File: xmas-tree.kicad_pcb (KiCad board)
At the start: 2 copper layers, 130.1 x 110 mm, 28 parts, among them U1 SN74HCS594, U2 LM555xM, U3 74AHC1G32

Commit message: Initial Commit
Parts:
- removed REF**: MountingHole_3.2mm_M3_DIN965_Pad, MountingHole:MountingHole_3.2mm_M3_DIN965_Pad
- C1: renamed from C2; value 0.1uf -> 0.01uf; footprint Capacitor_SMD:C_1210_3225Metric_Pad1.33x2.70mm_HandSolder -> Capacitor_SMD:C_0805_2012Metric_Pad1.18x1.45mm_HandSolder
- C2: renamed from C1; footprint Capacitor_SMD:C_1210_3225Metric_Pad1.33x2.70mm_HandSolder -> Capacitor_SMD:C_0805_2012Metric_Pad1.18x1.45mm_HandSolder
- C3: value C_Small -> 22uf; footprint Capacitor_SMD:C_1210_3225Metric_Pad1.33x2.70mm_HandSolder -> Capacitor_SMD:C_0805_2012Metric_Pad1.18x1.45mm_HandSolder
- D8: renamed from D4; moved to B.Cu
- R1: renamed from R7; footprint Resistor_SMD:R_2010_5025Metric -> Resistor_SMD:R_0805_2012Metric_Pad1.20x1.40mm_HandSolder
- R10: renamed from R6; value R_US -> 13K; footprint Resistor_SMD:R_2010_5025Metric_Pad1.40x2.65mm_HandSolder -> Resistor_SMD:R_0805_2012Metric_Pad1.20x1.40mm_HandSolder
- R2, R5: footprint Resistor_SMD:R_2010_5025Metric -> Resistor_SMD:R_0805_2012Metric_Pad1.20x1.40mm_HandSolder
- R3: renamed from R1; footprint Resistor_SMD:R_2010_5025Metric -> Resistor_SMD:R_0805_2012Metric_Pad1.20x1.40mm_HandSolder
- R4: renamed from R3; footprint Resistor_SMD:R_2010_5025Metric -> Resistor_SMD:R_0805_2012Metric_Pad1.20x1.40mm_HandSolder
- R6: renamed from R8; footprint Resistor_SMD:R_2010_5025Metric -> Resistor_SMD:R_0805_2012Metric_Pad1.20x1.40mm_HandSolder
- R7: renamed from R10; footprint Resistor_SMD:R_2010_5025Metric -> Resistor_SMD:R_0805_2012Metric_Pad1.20x1.40mm_HandSolder
- R8: renamed from R4; footprint Resistor_SMD:R_2010_5025Metric -> Resistor_SMD:R_0805_2012Metric_Pad1.20x1.40mm_HandSolder
- R9: value R_US -> 0; footprint Resistor_SMD:R_2010_5025Metric_Pad1.40x2.65mm_HandSolder -> Resistor_SMD:R_0805_2012Metric_Pad1.20x1.40mm_HandSolder
- turned D8 to 0 degrees
- renumbered D6 to D1, D1 to D2, D2 to D4, D7 to D6, D8 to D7
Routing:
- net LED_G: track 63.8 -> 71.4 mm
- net LED_F: track 59.3 -> 56.9 mm
- net Net-(C3-Pad1): track 27.1 -> 29.4 mm
- net LED_A: track 37.7 -> 35.9 mm
- net LED_H: track 18.4 -> 19.5 mm
- net VCC: track 152.0 -> 152.9 mm
- net Net-(R10-Pad1): track 19.4 -> 18.5 mm
- net Net-(D5-Pad2): track 5.98 -> 5.44 mm
- net Net-(D4-Pad2): track 5.07 -> 4.53 mm
- net Net-(D3-Pad2): track 5.71 -> 5.17 mm
- net LED_D: track 16.8 -> 16.3 mm
- net Net-(D8-Pad2): track 5.53 -> 4.99 mm
- net Net-(D7-Pad2): track 5.53 -> 4.99 mm
- net Net-(D6-Pad2): track 5.92 -> 5.37 mm
- net Net-(D2-Pad2): track 5.53 -> 4.99 mm
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
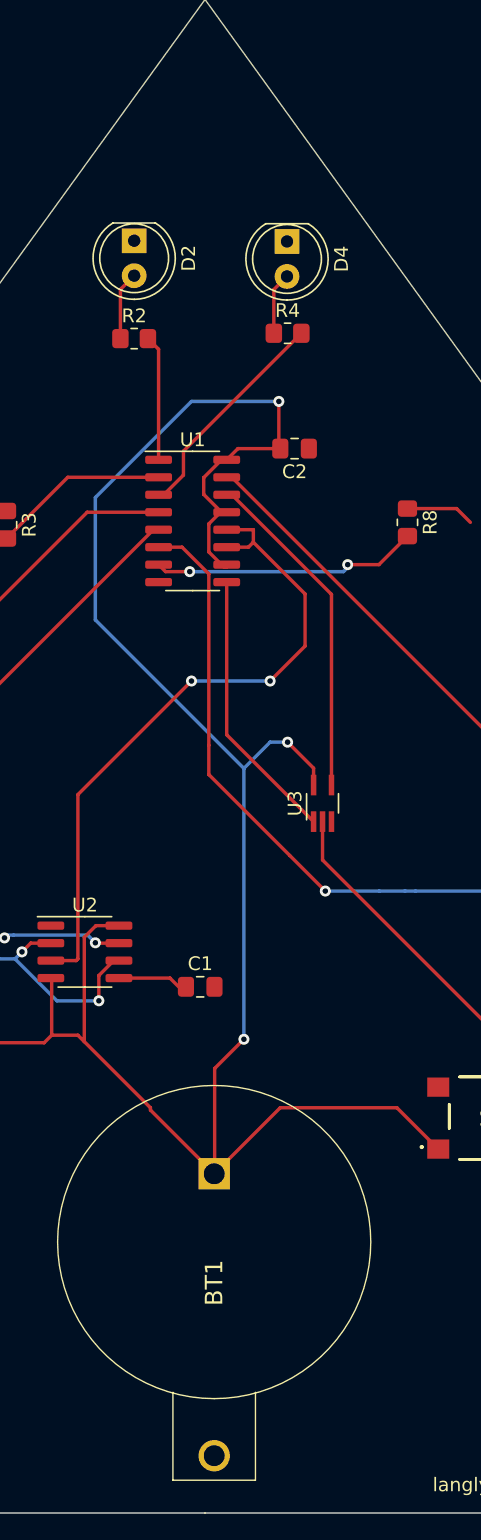
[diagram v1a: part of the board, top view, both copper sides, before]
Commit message: Fixed the problem of the battery holder being the wrong way
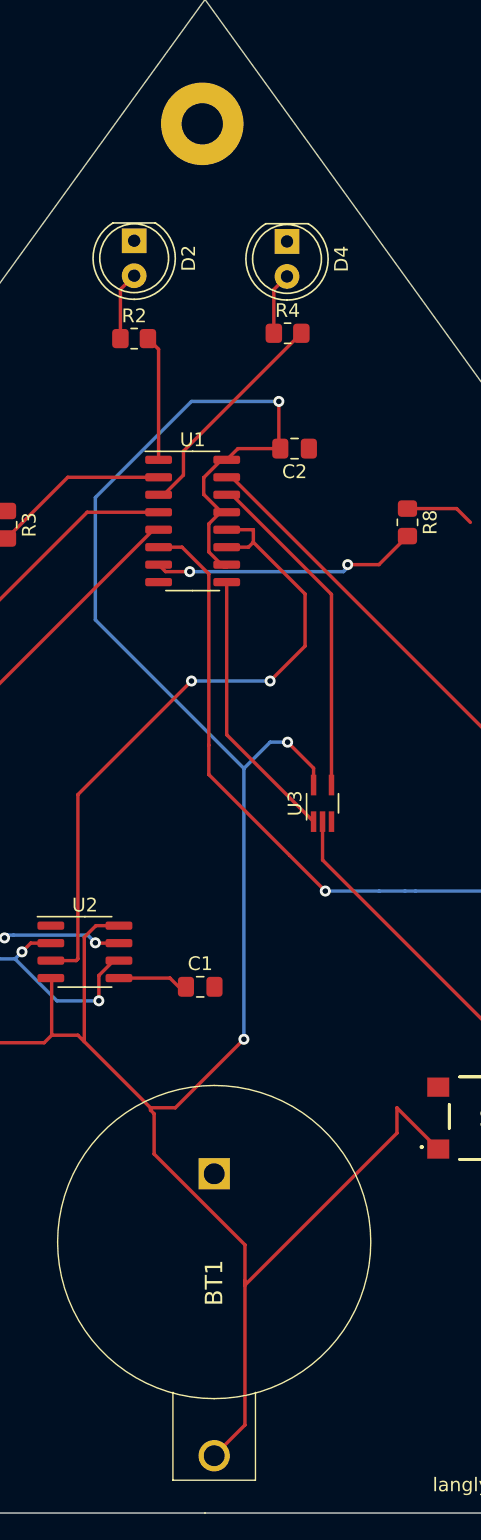
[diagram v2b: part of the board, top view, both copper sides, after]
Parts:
- added REF**: MountingHole_3mm_Pad, MountingHole:MountingHole_3mm_Pad, F.Cu at (158.5, 49.2)
- R9: value 0 -> 2k
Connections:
- BT1 pad 1: VCC -> GND
- BT1 pad 2: GND -> VCC
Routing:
- net VCC: track 152.9 -> 176.0 mm
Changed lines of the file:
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@@
     (fp_arc (start 16.34 0) (mid 4.96 11.38) (end -6.42 0) (layer "F.Fab") (width 0.2))
     (pad "1" thru_hole rect locked (at 0 0 270) (size 2.28 2.28) (drill 1.52) (layers *.Cu *.Mask)
-      (net 1 "VCC") (pinfunction "+") (pintype "passive"))
+      (net 2 "GND") (pinfunction "+") (pintype "passive"))
     (pad "2" thru_hole circle locked (at 20.49 0 270) (size 2.28 2.28) (drill 1.52) (layers *.Cu *.Mask)
-      (net 2 "GND") (pinfunction "-") (pintype "passive"))
+      (net 1 "VCC") (pinfunction "-") (pintype "passive"))
     (model "101.stp"
       (offset (xyz 0 0 0))
@@
     )
   )
+  (footprint "MountingHole:MountingHole_3mm_Pad" (layer "F.Cu")
+    (at 158.5 49.237)
+    (descr "Mounting Hole 3mm")
+    (tags "mounting hole 3mm")
+    (attr exclude_from_pos_files exclude_from_bom)
+    (fp_text reference "REF**" (at 0 -4) (layer "F.SilkS") hide
+      (effects (font (size 1 1) (thickness 0.15)))
+    )
+    (fp_text value "MountingHole_3mm_Pad" (at 0 4) (layer "F.Fab")
+      (effects (font (size 1 1) (thickness 0.15)))
+    )
+    (fp_text user "${REFERENCE}" (at 0.3 0) (layer "F.Fab")
+      (effects (font (size 1 1) (thickness 0.15)))
+    )
+    (fp_circle (center 0 0) (end 3 0) (layer "Cmts.User") (width 0.15) (fill none))
+    (fp_circle (center 0 0) (end 3.25 0) (layer "F.CrtYd") (width 0.05) (fill none))
+    (pad "1" thru_hole circle (at 0 0) (size 6 6) (drill 3) (layers *.Cu *.Mask))
+  )
   (footprint "Package_SO:SOIC-16_3.9x9.9mm_P1.27mm" (layer "F.Cu")
     (at 157.8 78.1)
@@
       (effects (font (size 1 1) (thickness 0.15)))
     )
-    (fp_text value "0" (at 0 1.65 180) (layer "F.Fab")
+    (fp_text value "2k" (at 0 1.65 180) (layer "F.Fab")
       (effects (font (size 1 1) (thickness 0.15)))
     )
@@
     (effects (font (size 1 1) (thickness 0.15)))
   )
+  (segment (start 161.525 115.767) (end 156.544416 120.747584) (width 0.25) (layer "F.Cu") (net 1))
   (segment (start 147.555 115.4745) (end 147.555 111.384) (width 0.25) (layer "F.Cu") (net 1))
   (segment (start 141.824 116.021) (end 147.0085 116.021) (width 0.25) (layer "F.Cu") (net 1))
   (segment (start 149.46 115.4745) (end 147.555 115.4745) (width 0.25) (layer "F.Cu") (net 1))
-  (segment (start 164.164416 120.747584) (end 172.647584 120.747584) (width 0.25) (layer "F.Cu") (net 1))
+  (segment (start 161.599478 143.802522) (end 161.599478 133.336478) (width 0.25) (layer "F.Cu") (net 1))
   (segment (start 150.7685 107.512) (end 152.443 107.512) (width 0.25) (layer "F.Cu") (net 1))
+  (segment (start 155 124.109022) (end 161.599478 130.7085) (width 0.25) (layer "F.Cu") (net 1))
+  (segment (start 149.92375 115.93825) (end 154.733084 120.747584) (width 0.25) (layer "F.Cu") (net 1))
   (segment (start 158.97548 78.31152) (end 159.822 77.465) (width 0.25) (layer "F.Cu") (net 1))
   (segment (start 163.6455 72.841) (end 161.089 72.841) (width 0.25) (layer "F.Cu") (net 1))
   (segment (start 164.7 94.177) (end 166.59 96.067) (width 0.25) (layer "F.Cu") (net 1))
+  (segment (start 161.599478 130.7085) (end 161.599478 133.336478) (width 0.25) (layer "F.Cu") (net 1))
   (segment (start 158.97548 80.351552) (end 158.97548 78.31152) (width 0.25) (layer "F.Cu") (net 1))
+  (segment (start 154.733084 120.747584) (end 154.733084 120.913084) (width 0.25) (layer "F.Cu") (net 1))
   (segment (start 160.275 81.275) (end 160.275 81.457) (width 0.25) (layer "F.Cu") (net 1))
   (segment (start 159.822 77.465) (end 160.275 77.465) (width 0.25) (layer "F.Cu") (net 1))
   (segment (start 149.92375 115.93825) (end 149.46 115.4745) (width 0.25) (layer "F.Cu") (net 1))
-  (segment (start 154.733084 120.913084) (end 154.733084 120.747584) (width 0.25) (layer "F.Cu") (net 1))
   (segment (start 158.604 74.949928) (end 158.604 76.170072) (width 0.25) (layer "F.Cu") (net 1))
   (segment (start 149.92375 108.35675) (end 150.7685 107.512) (width 0.25) (layer "F.Cu") (net 1))
-  (segment (start 159.4 117.892) (end 161.525 115.767) (width 0.25) (layer "F.Cu") (net 1))
-  (segment (start 154.733084 120.747584) (end 149.92375 115.93825) (width 0.25) (layer "F.Cu") (net 1))
+  (segment (start 159.366 146.036) (end 161.599478 143.802522) (width 0.25) (layer "F.Cu") (net 1))
+  (segment (start 154.733084 120.913084) (end 155 121.18) (width 0.25) (layer "F.Cu") (net 1))
   (segment (start 159.898928 73.655) (end 158.604 74.949928) (width 0.25) (layer "F.Cu") (net 1))
   (segment (start 149.92375 115.93825) (end 149.92375 108.35675) (width 0.25) (layer "F.Cu") (net 1))
-  (segment (start 159.366 125.546) (end 154.733084 120.913084) (width 0.25) (layer "F.Cu") (net 1))
   (segment (start 158.604 76.170072) (end 159.898928 77.465) (width 0.25) (layer "F.Cu") (net 1))
   (segment (start 160.275 81.457) (end 160.080928 81.457) (width 0.25) (layer "F.Cu") (net 1))
+  (segment (start 172.647584 120.747584) (end 175.65 123.75) (width 0.25) (layer "F.Cu") (net 1))
+  (segment (start 161.599478 133.336478) (end 161.599478 133.637522) (width 0.25) (layer "F.Cu") (net 1))
   (segment (start 160.080928 81.457) (end 158.97548 80.351552) (width 0.25) (layer "F.Cu") (net 1))
-  (segment (start 159.4 125.512) (end 159.4 117.892) (width 0.25) (layer "F.Cu") (net 1))
+  (segment (start 155 121.18) (end 155 124.109022) (width 0.25) (layer "F.Cu") (net 1))
+  (segment (start 161.599478 133.637522) (end 172.647584 122.589416) (width 0.25) (layer "F.Cu") (net 1))
   (segment (start 166.59 96.067) (end 166.59 97.292) (width 0.25) (layer "F.Cu") (net 1))
   (segment (start 160.275 73.655) (end 159.898928 73.655) (width 0.25) (layer "F.Cu") (net 1))
-  (segment (start 172.647584 120.747584) (end 175.65 123.75) (width 0.25) (layer "F.Cu") (net 1))
   (segment (start 161.089 72.841) (end 160.275 73.655) (width 0.25) (layer "F.Cu") (net 1))
   (segment (start 164.065 69.412) (end 164.065 72.4215) (width 0.25) (layer "F.Cu") (net 1))
+  (segment (start 172.647584 122.589416) (end 172.647584 120.747584) (width 0.25) (layer "F.Cu") (net 1))
   (segment (start 164.065 72.4215) (end 163.6455 72.841) (width 0.25) (layer "F.Cu") (net 1))
   (segment (start 147.0085 116.021) (end 147.555 115.4745) (width 0.25) (layer "F.Cu") (net 1))
-  (segment (start 159.366 125.546) (end 164.164416 120.747584) (width 0.25) (layer "F.Cu") (net 1))
+  (segment (start 156.544416 120.747584) (end 154.733084 120.747584) (width 0.25) (layer "F.Cu") (net 1))
   (segment (start 147.555 111.384) (end 147.493 111.322) (width 0.25) (layer "F.Cu") (net 1))
   (via (at 164.065 69.412) (size 0.8) (drill 0.4) (layers "F.Cu" "B.Cu") (net 1))
